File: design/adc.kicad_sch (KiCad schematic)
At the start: 27 parts, among them J6 JUMPER_DFS/GAIN, U11 TLV431ACDBZR, U12 AD9214

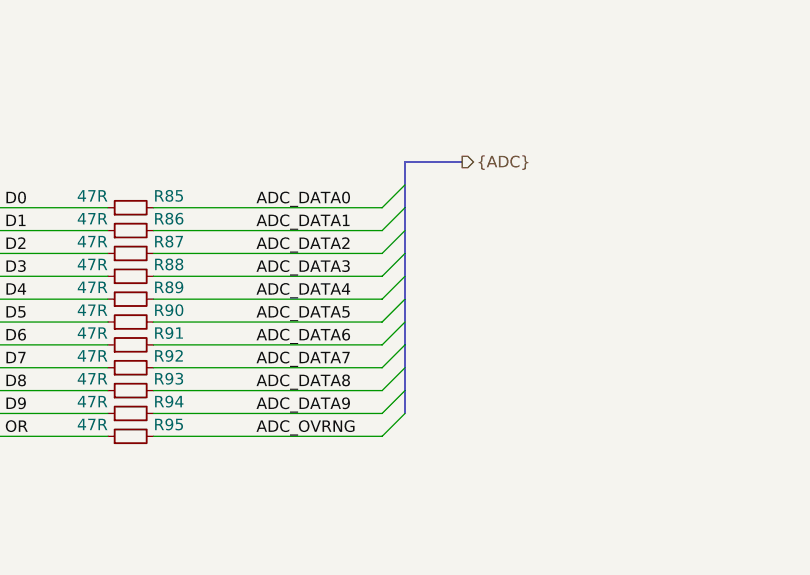
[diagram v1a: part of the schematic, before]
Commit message: Refactored FPGA schematic
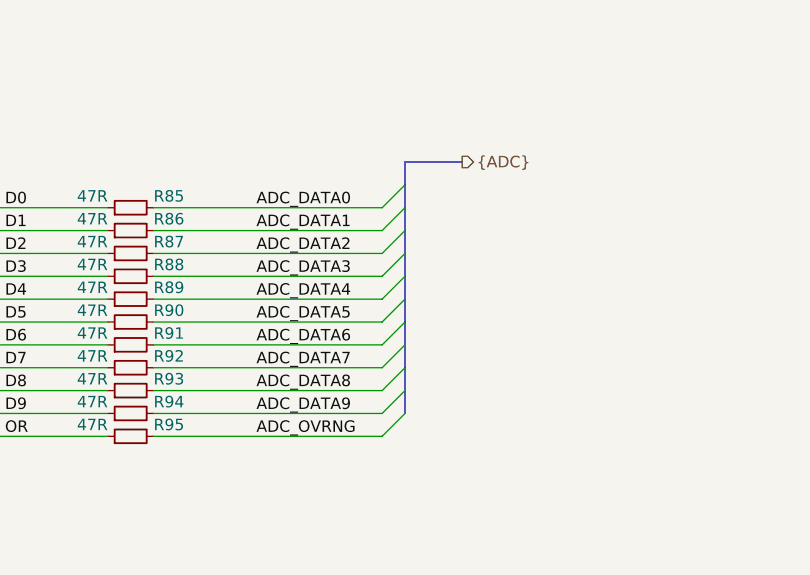
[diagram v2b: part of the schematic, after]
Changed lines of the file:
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@@
-(kicad_sch (version 20200512) (host eeschema "5.99.0-unknown-ad88874~101~ubuntu18.04.1")
-  (page 7 8)
+(kicad_sch (version 20200512) (host eeschema "5.99.0-unknown-92ce7ca~101~ubuntu18.04.1")
+  (page 1 8)
   (paper "A4")
   (title_block
@@
   (wire (pts (xy 270.51 53.34) (xy 270.51 54.61)))
   (wire (pts (xy 270.51 62.23) (xy 270.51 63.5)))
-  (bus (pts (xy 214.63 88.9) (xy 214.63 93.98)))
-  (bus (pts (xy 214.63 93.98) (xy 214.63 99.06)))
-  (bus (pts (xy 214.63 99.06) (xy 214.63 104.14)))
-  (bus (pts (xy 214.63 104.14) (xy 214.63 109.22)))
-  (bus (pts (xy 214.63 109.22) (xy 214.63 114.3)))
-  (bus (pts (xy 214.63 114.3) (xy 214.63 116.84)))
+  (bus (pts (xy 214.63 88.9) (xy 214.63 91.44)))
+  (bus (pts (xy 214.63 91.44) (xy 214.63 96.52)))
+  (bus (pts (xy 214.63 96.52) (xy 214.63 101.6)))
+  (bus (pts (xy 214.63 101.6) (xy 214.63 106.68)))
+  (bus (pts (xy 214.63 106.68) (xy 214.63 111.76)))
+  (bus (pts (xy 214.63 111.76) (xy 214.63 116.84)))
   (bus (pts (xy 220.98 88.9) (xy 214.63 88.9)))
   (text "1.24V" (at 40.64 36.83 180)

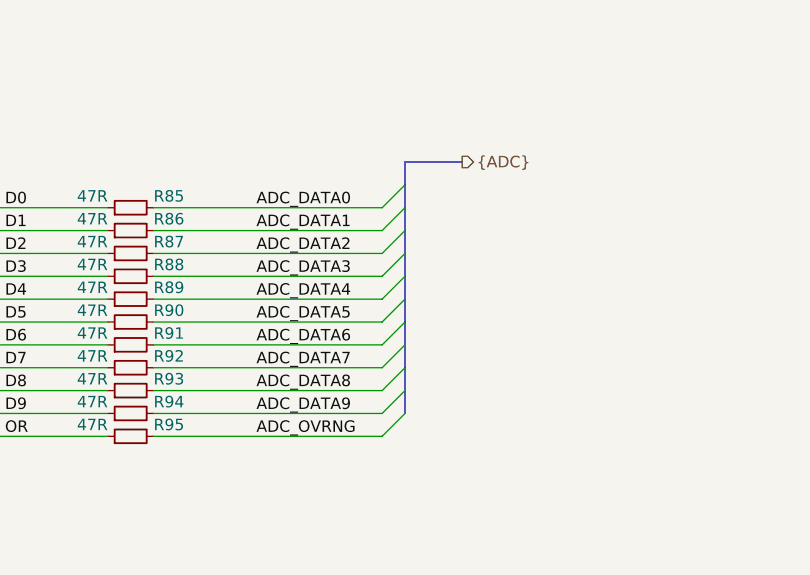
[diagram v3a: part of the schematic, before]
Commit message: Added oscilator layout
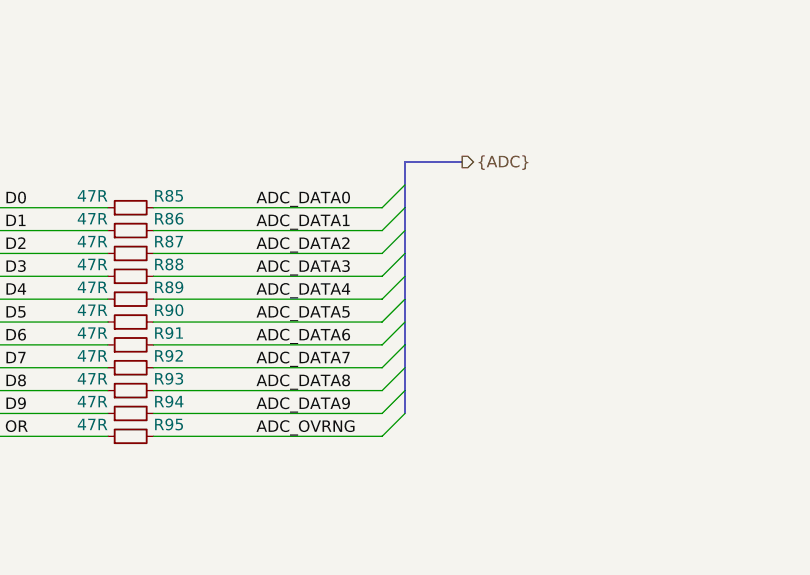
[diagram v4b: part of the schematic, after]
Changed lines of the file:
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@@
-(kicad_sch (version 20200512) (host eeschema "5.99.0-unknown-92ce7ca~101~ubuntu18.04.1")
+(kicad_sch (version 20200512) (host eeschema "5.99.0-unknown-0658d29~101~ubuntu18.04.1")
   (page 7 8)
   (paper "A4")
@@
   (wire (pts (xy 270.51 53.34) (xy 270.51 54.61)))
   (wire (pts (xy 270.51 62.23) (xy 270.51 63.5)))
-  (bus (pts (xy 214.63 88.9) (xy 214.63 91.44)))
-  (bus (pts (xy 214.63 91.44) (xy 214.63 96.52)))
-  (bus (pts (xy 214.63 96.52) (xy 214.63 101.6)))
-  (bus (pts (xy 214.63 101.6) (xy 214.63 106.68)))
-  (bus (pts (xy 214.63 106.68) (xy 214.63 111.76)))
-  (bus (pts (xy 214.63 111.76) (xy 214.63 116.84)))
+  (bus (pts (xy 214.63 88.9) (xy 214.63 93.98)))
+  (bus (pts (xy 214.63 93.98) (xy 214.63 99.06)))
+  (bus (pts (xy 214.63 99.06) (xy 214.63 104.14)))
+  (bus (pts (xy 214.63 104.14) (xy 214.63 109.22)))
+  (bus (pts (xy 214.63 109.22) (xy 214.63 114.3)))
+  (bus (pts (xy 214.63 114.3) (xy 214.63 116.84)))
   (bus (pts (xy 220.98 88.9) (xy 214.63 88.9)))
   (text "1.24V" (at 40.64 36.83 180)

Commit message: Added FTDI RST support
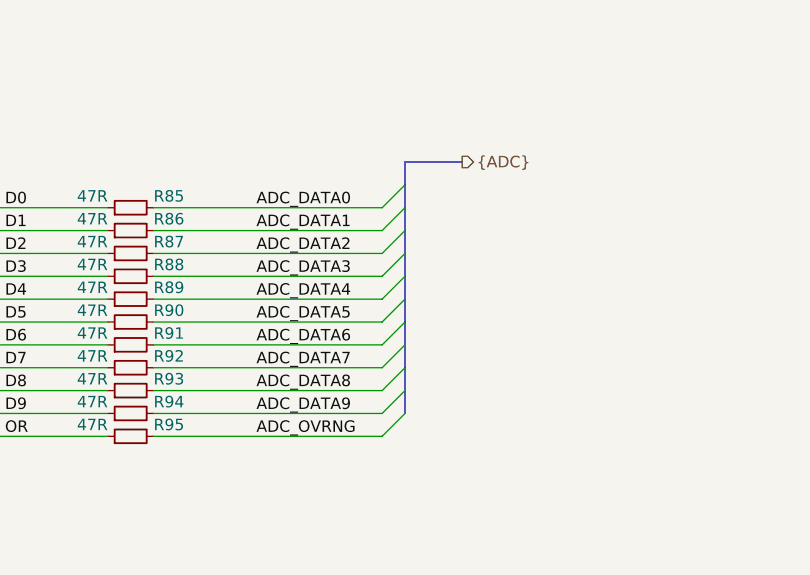
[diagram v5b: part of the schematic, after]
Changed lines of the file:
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@@
-(kicad_sch (version 20200512) (host eeschema "5.99.0-unknown-0658d29~101~ubuntu18.04.1")
-  (page 7 8)
+(kicad_sch (version 20200512) (host eeschema "5.99.0-unknown-d72a778~101~ubuntu18.04.1")
+  (page 1 8)
   (paper "A4")
   (title_block
@@
   (wire (pts (xy 270.51 53.34) (xy 270.51 54.61)))
   (wire (pts (xy 270.51 62.23) (xy 270.51 63.5)))
-  (bus (pts (xy 214.63 88.9) (xy 214.63 93.98)))
-  (bus (pts (xy 214.63 93.98) (xy 214.63 99.06)))
-  (bus (pts (xy 214.63 99.06) (xy 214.63 104.14)))
-  (bus (pts (xy 214.63 104.14) (xy 214.63 109.22)))
-  (bus (pts (xy 214.63 109.22) (xy 214.63 114.3)))
-  (bus (pts (xy 214.63 114.3) (xy 214.63 116.84)))
+  (bus (pts (xy 214.63 88.9) (xy 214.63 91.44)))
+  (bus (pts (xy 214.63 91.44) (xy 214.63 96.52)))
+  (bus (pts (xy 214.63 96.52) (xy 214.63 101.6)))
+  (bus (pts (xy 214.63 101.6) (xy 214.63 106.68)))
+  (bus (pts (xy 214.63 106.68) (xy 214.63 111.76)))
+  (bus (pts (xy 214.63 111.76) (xy 214.63 116.84)))
   (bus (pts (xy 220.98 88.9) (xy 214.63 88.9)))
   (text "1.24V" (at 40.64 36.83 180)

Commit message: Fixed MCU RST
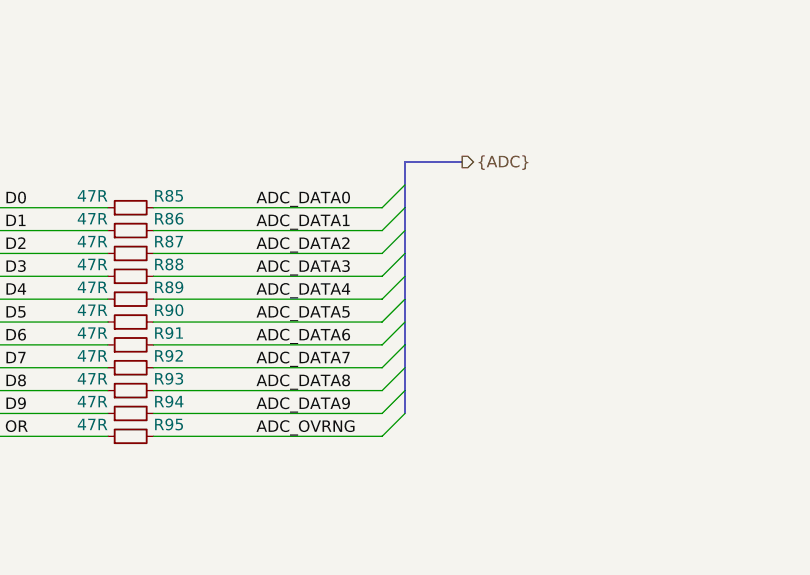
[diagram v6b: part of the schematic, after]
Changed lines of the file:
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@@
   (wire (pts (xy 270.51 53.34) (xy 270.51 54.61)))
   (wire (pts (xy 270.51 62.23) (xy 270.51 63.5)))
-  (bus (pts (xy 214.63 88.9) (xy 214.63 91.44)))
-  (bus (pts (xy 214.63 91.44) (xy 214.63 96.52)))
-  (bus (pts (xy 214.63 96.52) (xy 214.63 101.6)))
-  (bus (pts (xy 214.63 101.6) (xy 214.63 106.68)))
-  (bus (pts (xy 214.63 106.68) (xy 214.63 111.76)))
-  (bus (pts (xy 214.63 111.76) (xy 214.63 116.84)))
+  (bus (pts (xy 214.63 88.9) (xy 214.63 93.98)))
+  (bus (pts (xy 214.63 93.98) (xy 214.63 99.06)))
+  (bus (pts (xy 214.63 99.06) (xy 214.63 104.14)))
+  (bus (pts (xy 214.63 104.14) (xy 214.63 109.22)))
+  (bus (pts (xy 214.63 109.22) (xy 214.63 114.3)))
+  (bus (pts (xy 214.63 114.3) (xy 214.63 116.84)))
   (bus (pts (xy 220.98 88.9) (xy 214.63 88.9)))
   (text "1.24V" (at 40.64 36.83 180)

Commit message: Updated some layout
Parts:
- renumbered C57 to C61, C58 to C62, C59 to C63, C60 to C64, C61 to C65, C62 to C66, C63 to C67, C64 to C68, C65 to C69, C66 to C70, C67 to C71, C68 to C72, R84 to R87, R85 to R88, R86 to R89, R87 to R90, R88 to R91, R89 to R92, R90 to R93, R91 to R94, R92 to R95, R93 to R96, R94 to R97, R95 to R98, U11 to U12, U12 to U13

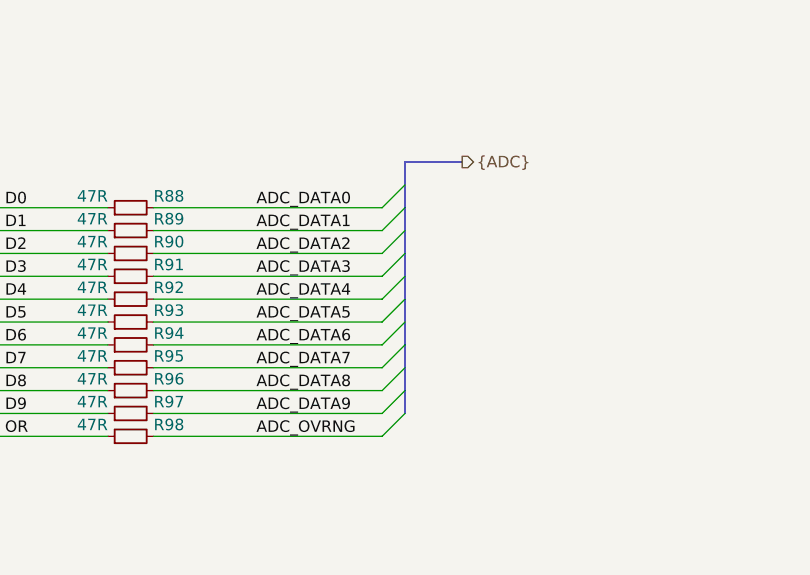
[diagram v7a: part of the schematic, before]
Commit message: Added logo and description to F.Silks
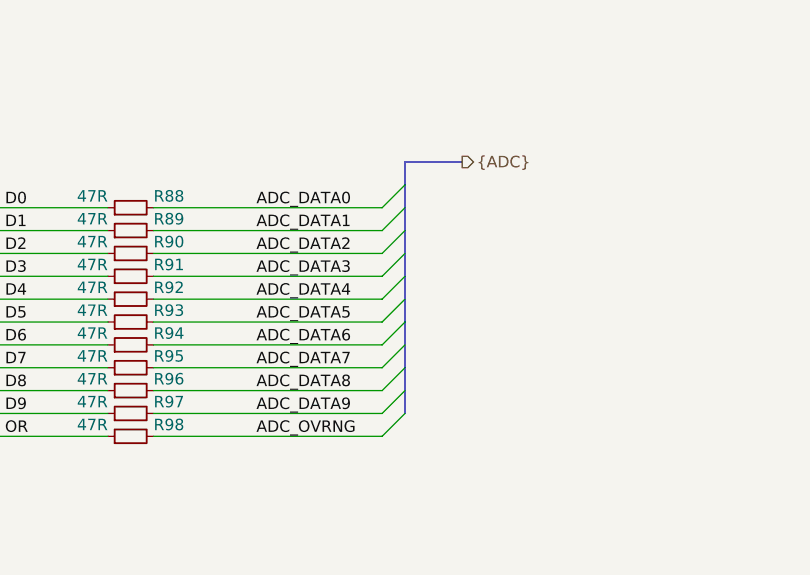
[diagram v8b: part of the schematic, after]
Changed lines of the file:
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@@
-(kicad_sch (version 20200512) (host eeschema "5.99.0-unknown-d72a778~101~ubuntu18.04.1")
+(kicad_sch (version 20200512) (host eeschema "5.99.0-unknown-4efed4b~101~ubuntu18.04.1")
   (page 7 8)
   (paper "A4")
@@
   (wire (pts (xy 270.51 53.34) (xy 270.51 54.61)))
   (wire (pts (xy 270.51 62.23) (xy 270.51 63.5)))
-  (bus (pts (xy 214.63 88.9) (xy 214.63 93.98)))
-  (bus (pts (xy 214.63 93.98) (xy 214.63 99.06)))
-  (bus (pts (xy 214.63 99.06) (xy 214.63 104.14)))
-  (bus (pts (xy 214.63 104.14) (xy 214.63 109.22)))
-  (bus (pts (xy 214.63 109.22) (xy 214.63 114.3)))
-  (bus (pts (xy 214.63 114.3) (xy 214.63 116.84)))
+  (bus (pts (xy 214.63 88.9) (xy 214.63 91.44)))
+  (bus (pts (xy 214.63 91.44) (xy 214.63 96.52)))
+  (bus (pts (xy 214.63 96.52) (xy 214.63 101.6)))
+  (bus (pts (xy 214.63 101.6) (xy 214.63 106.68)))
+  (bus (pts (xy 214.63 106.68) (xy 214.63 111.76)))
+  (bus (pts (xy 214.63 111.76) (xy 214.63 116.84)))
   (bus (pts (xy 220.98 88.9) (xy 214.63 88.9)))
   (text "1.24V" (at 40.64 36.83 180)
